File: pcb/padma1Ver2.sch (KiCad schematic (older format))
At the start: 12 parts

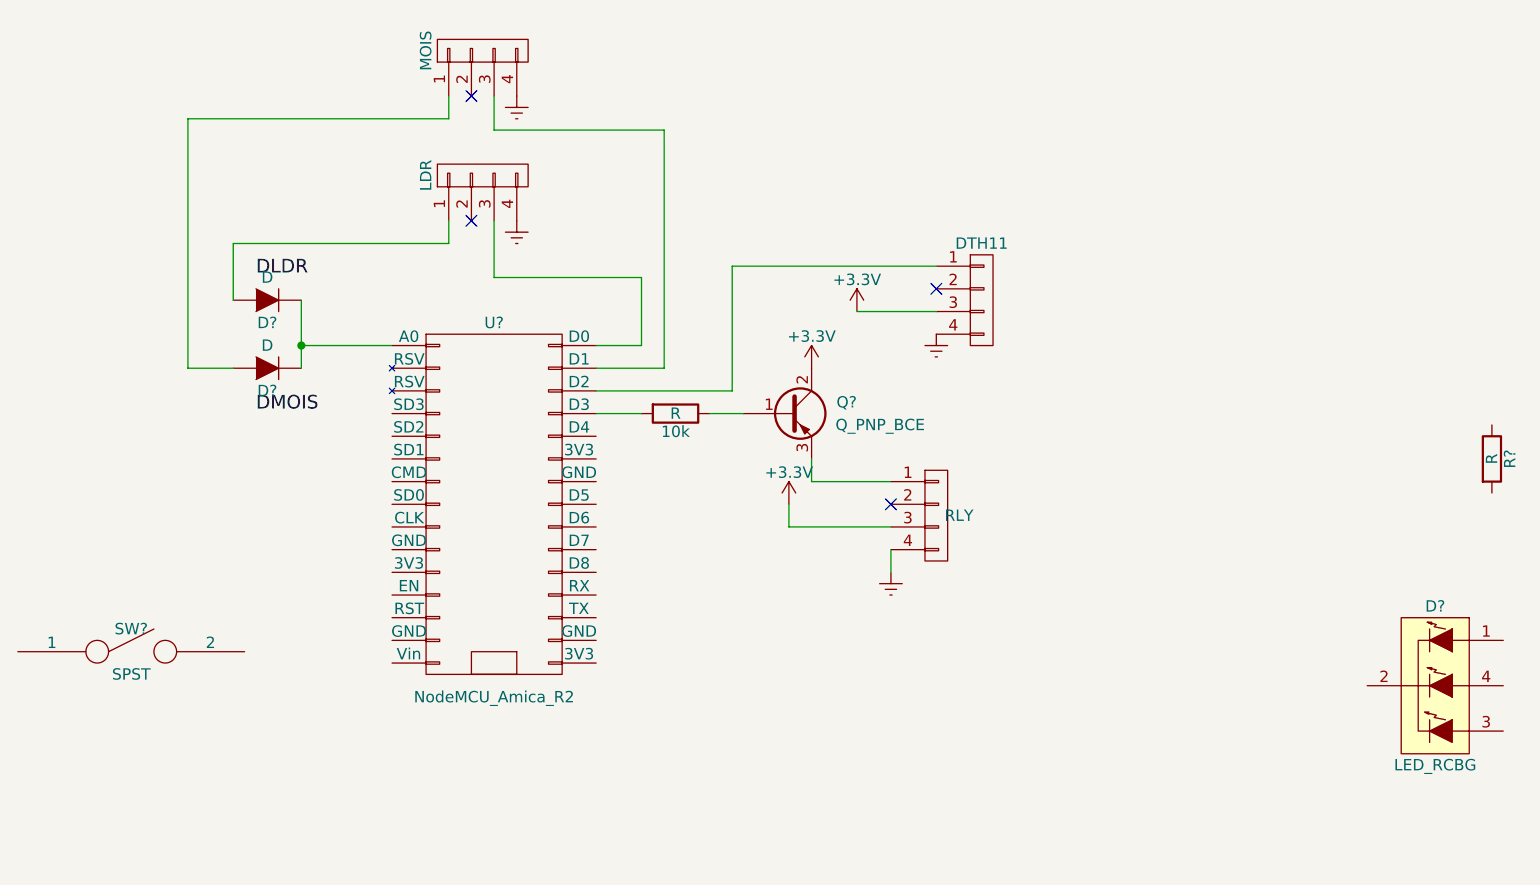
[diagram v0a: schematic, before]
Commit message: schematic completed
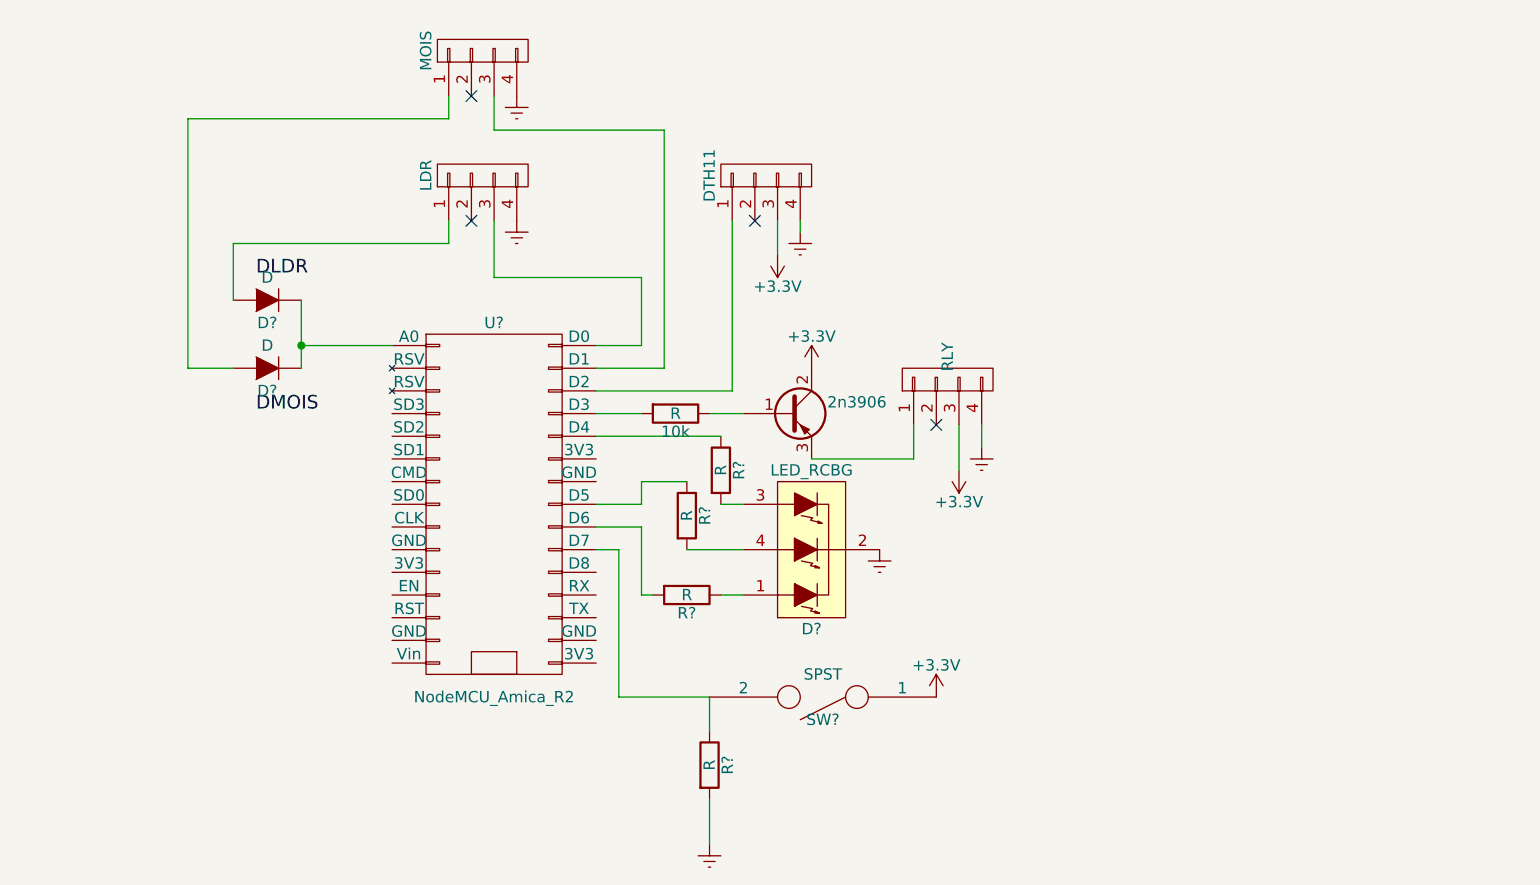
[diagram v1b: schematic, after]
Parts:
- added R? (x3): R, symbol R
- gave numbers to parts that had none: 1
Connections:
- net +3V3: now also SW?.1
- net Earth: now also D?.2 (COMMON_CATHODE), R?.2
- net at U?.21 (D7): now also R?.1, SW?.2
- net at U?.22 (D6): now also R?.2
- net at U?.23 (D5): now also R?.1
- net at U?.26 (D4): now also R?.1
- net at D?.1 (RED_ANODE): now also R?.1
- net at D?.3 (BLUE_ANODE): now also R?.2
- net at D?.4 (GREEN_ANODE): now also R?.2
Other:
- moved on the sheet: D?, DTH11, R?, SW?
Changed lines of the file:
@@
 L R R?
 U 1 1 582C3672
-P 9050 3300
-F 0 "R?" V 9130 3300 50  0000 C CNN
-F 1 "R" V 9050 3300 50  0000 C CNN
-F 2 "" V 8980 3300 50  0000 C CNN
-F 3 "" H 9050 3300 50  0000 C CNN
-	1    9050 3300
+P 5600 4650
+F 0 "R?" V 5680 4650 50  0000 C CNN
+F 1 "R" V 5600 4650 50  0000 C CNN
+F 2 "" V 5530 4650 50  0000 C CNN
+F 3 "" H 5600 4650 50  0000 C CNN
+	1    5600 4650
 	1    0    0    -1
 $EndComp
@@
 $EndComp
 $Comp
-L Q_PNP_BCE Q?
+L Q_PNP_BCE 2n3906
 U 1 1 582C37C4
 P 5950 3100
-F 0 "Q?" H 6250 3150 50  0000 R CNN
-F 1 "Q_PNP_BCE" H 6550 3050 50  0000 R CNN
+F 0 "2n3906" H 6250 3150 50  0000 C CNN
+F 1 "Q_PNP_BCE" H 6550 3050 50  0001 R CNN
 F 2 "" H 6150 3200 50  0000 C CNN
 F 3 "" H 5950 3100 50  0000 C CNN
@@
 L SPST SW?
 U 1 1 582C382D
-P 3050 4150
-F 0 "SW?" H 3050 4250 50  0000 C CNN
-F 1 "SPST" H 3050 4050 50  0000 C CNN
-F 2 "" H 3050 4150 50  0000 C CNN
-F 3 "" H 3050 4150 50  0000 C CNN
-	1    3050 4150
-	1    0    0    -1
-$EndComp
-$Comp
-L LED_RCBG D?
-U 1 1 582C388A
-P 8800 4300
-F 0 "D?" H 8800 4650 50  0000 C CNN
-F 1 "LED_RCBG" H 8800 3950 50  0000 C CNN
-F 2 "" H 8800 4250 50  0000 C CNN
-F 3 "" H 8800 4250 50  0000 C CNN
-	1    8800 4300
-	1    0    0    -1
+P 6100 4350
+F 0 "SW?" H 6100 4450 50  0000 C CNN
+F 1 "SPST" H 6100 4250 50  0000 C CNN
+F 2 "" H 6100 4350 50  0000 C CNN
+F 3 "" H 6100 4350 50  0000 C CNN
+	1    6100 4350
+	-1   0    0    1
 $EndComp
 $Comp
@@
 	-1   0    0    1
 $EndComp
-Wire Wire Line
-	3800 2600 3800 2900
-Wire Wire Line
-	4200 2800 3800 2800
-Connection ~ 3800 2800
 $Comp
 L CONN_01X04 LDR
@@
 L CONN_01X04 DTH11
 U 1 1 582C4013
-P 6800 2600
-F 0 "DTH11" H 6800 2850 50  0000 C CNN
-F 1 "CONN_01X04" V 6900 2600 50  0001 C CNN
-F 2 "" H 6800 2600 50  0000 C CNN
-F 3 "" H 6800 2600 50  0000 C CNN
-	1    6800 2600
-	1    0    0    -1
+P 5850 2050
+F 0 "DTH11" H 5850 2300 50  0000 C CNN
+F 1 "CONN_01X04" V 5950 2050 50  0001 C CNN
+F 2 "" H 5850 2050 50  0000 C CNN
+F 3 "" H 5850 2050 50  0000 C CNN
+	1    5850 2050
+	0    -1   -1   0
 $EndComp
 $Comp
 L CONN_01X04 Grovr
 U 1 1 582C406C
-P 6600 3550
-F 0 "Grovr" H 6600 3800 50  0001 C CNN
-F 1 "RLY" H 6700 3550 50  0000 C CNN
-F 2 "" H 6600 3550 50  0000 C CNN
-F 3 "" H 6600 3550 50  0000 C CNN
-	1    6600 3550
-	1    0    0    -1
+P 6650 2950
+F 0 "Grovr" H 6650 3200 50  0001 C CNN
+F 1 "RLY" H 6750 2950 50  0000 C CNN
+F 2 "" H 6650 2950 50  0000 C CNN
+F 3 "" H 6650 2950 50  0000 C CNN
+	1    6650 2950
+	0    -1   -1   0
 $EndComp
 Text Label 3600 2500 0    60   ~ 0
@@
 Text Label 3600 3100 0    60   ~ 0
 DMOIS
-Wire Wire Line
-	3500 2600 3500 2350
-Wire Wire Line
-	3300 2900 3500 2900
-Wire Wire Line
-	3300 1800 3300 2900
-Wire Wire Line
-	3300 1800 4450 1800
-Wire Wire Line
-	4450 1800 4450 1700
-Wire Wire Line
-	3500 2350 4450 2350
-Wire Wire Line
-	4450 2350 4450 2250
 NoConn ~ 4550 2250
 NoConn ~ 4550 1700
-Wire Wire Line
-	5100 2800 5300 2800
-Wire Wire Line
-	5300 2800 5300 2500
-Wire Wire Line
-	5300 2500 4650 2500
-Wire Wire Line
-	4650 2500 4650 2250
-Wire Wire Line
-	5100 2900 5400 2900
 $Comp
 L Earth #PWR?
@@
 	1    0    0    -1
 $EndComp
-$Comp
-L Earth #PWR?
-U 1 1 582C4E32
-P 6600 2750
-F 0 "#PWR?" H 6600 2500 50  0001 C CNN
-F 1 "Earth" H 6600 2600 50  0001 C CNN
-F 2 "" H 6600 2750 50  0000 C CNN
-F 3 "" H 6600 2750 50  0000 C CNN
-	1    6600 2750
-	1    0    0    -1
-$EndComp
-NoConn ~ 6600 2550
-$Comp
-L +3.3V #PWR?
-U 1 1 582C4FDC
-P 6250 2650
-F 0 "#PWR?" H 6250 2500 50  0001 C CNN
-F 1 "+3.3V" H 6250 2790 50  0000 C CNN
-F 2 "" H 6250 2650 50  0000 C CNN
-F 3 "" H 6250 2650 50  0000 C CNN
-	1    6250 2650
-	1    0    0    -1
-$EndComp
-Wire Wire Line
-	6600 2650 6250 2650
-Wire Wire Line
-	5100 3000 5700 3000
-Wire Wire Line
-	5700 3000 5700 2450
-Wire Wire Line
-	5700 2450 6600 2450
-Wire Wire Line
-	5100 3100 5300 3100
-Wire Wire Line
-	5600 3100 5750 3100
 $Comp
 L +3.3V #PWR?
@@
 	1    0    0    -1
 $EndComp
-Wire Wire Line
-	6050 3300 6050 3400
-Wire Wire Line
-	6050 3400 6400 3400
-Wire Wire Line
-	4650 1700 4650 1850
-Wire Wire Line
-	4650 1850 5400 1850
-Wire Wire Line
-	5400 1850 5400 2900
 $Comp
 L Earth #PWR?
@@
 	1    0    0    -1
 $EndComp
-NoConn ~ 6400 3500
+NoConn ~ 5800 2250
 $Comp
 L +3.3V #PWR?
-U 1 1 582C6CAC
-P 5950 3500
-F 0 "#PWR?" H 5950 3350 50  0001 C CNN
-F 1 "+3.3V" H 5950 3640 50  0000 C CNN
-F 2 "" H 5950 3500 50  0000 C CNN
-F 3 "" H 5950 3500 50  0000 C CNN
-	1    5950 3500
-	1    0    0    -1
-$EndComp
-$Comp
-L Earth #PWR?
-U 1 1 582C6D84
-P 6400 3800
-F 0 "#PWR?" H 6400 3550 50  0001 C CNN
-F 1 "Earth" H 6400 3650 50  0001 C CNN
-F 2 "" H 6400 3800 50  0000 C CNN
-F 3 "" H 6400 3800 50  0000 C CNN
-	1    6400 3800
-	1    0    0    -1
-$EndComp
-Wire Wire Line
-	6400 3700 6400 3800
-Wire Wire Line
-	5950 3600 6400 3600
-Wire Wire Line
-	5950 3500 5950 3600
+U 1 1 582C7499
+P 5900 2400
+F 0 "#PWR?" H 5900 2250 50  0001 C CNN
+F 1 "+3.3V" H 5900 2540 50  0000 C CNN
+F 2 "" H 5900 2400 50  0000 C CNN
+F 3 "" H 5900 2400 50  0000 C CNN
+	1    5900 2400
+	-1   0    0    1
+$EndComp
+$Comp
+L Earth #PWR?
+U 1 1 582C7550
+P 6000 2300
+F 0 "#PWR?" H 6000 2050 50  0001 C CNN
+F 1 "Earth" H 6000 2150 50  0001 C CNN
+F 2 "" H 6000 2300 50  0000 C CNN
+F 3 "" H 6000 2300 50  0000 C CNN
+	1    6000 2300
+	1    0    0    -1
+$EndComp
+NoConn ~ 6600 3150
+$Comp
+L +3.3V #PWR?
+U 1 1 582C78ED
+P 6700 3350
+F 0 "#PWR?" H 6700 3200 50  0001 C CNN
+F 1 "+3.3V" H 6700 3490 50  0000 C CNN
+F 2 "" H 6700 3350 50  0000 C CNN
+F 3 "" H 6700 3350 50  0000 C CNN
+	1    6700 3350
+	-1   0    0    1
+$EndComp
+$Comp
+L Earth #PWR?
+U 1 1 582C79CF
+P 6800 3250
+F 0 "#PWR?" H 6800 3000 50  0001 C CNN
+F 1 "Earth" H 6800 3100 50  0001 C CNN
+F 2 "" H 6800 3250 50  0000 C CNN
+F 3 "" H 6800 3250 50  0000 C CNN
+	1    6800 3250
+	1    0    0    -1
+$EndComp
+$Comp
+L LED_RCBG D?
+U 1 1 582C388A
+P 6050 3700
+F 0 "D?" H 6050 4050 50  0000 C CNN
+F 1 "LED_RCBG" H 6050 3350 50  0000 C CNN
+F 2 "" H 6050 3650 50  0000 C CNN
+F 3 "" H 6050 3650 50  0000 C CNN
+	1    6050 3700
+	-1   0    0    1
+$EndComp
+$Comp
+L R R?
+U 1 1 582C8339
+P 5650 3350
+F 0 "R?" V 5730 3350 50  0000 C CNN
+F 1 "R" V 5650 3350 50  0000 C CNN
+F 2 "" V 5580 3350 50  0000 C CNN
+F 3 "" H 5650 3350 50  0000 C CNN
+	1    5650 3350
+	1    0    0    -1
+$EndComp
+$Comp
+L R R?
+U 1 1 582C866A
+P 5500 3550
+F 0 "R?" V 5580 3550 50  0000 C CNN
+F 1 "R" V 5500 3550 50  0000 C CNN
+F 2 "" V 5430 3550 50  0000 C CNN
+F 3 "" H 5500 3550 50  0000 C CNN
+	1    5500 3550
+	1    0    0    -1
+$EndComp
+$Comp
+L R R?
+U 1 1 582C8997
+P 5500 3900
+F 0 "R?" V 5580 3900 50  0000 C CNN
+F 1 "R" V 5500 3900 50  0000 C CNN
+F 2 "" V 5430 3900 50  0000 C CNN
+F 3 "" H 5500 3900 50  0000 C CNN
+	1    5500 3900
+	0    1    1    0
+$EndComp
+$Comp
+L Earth #PWR?
+U 1 1 582C8C6A
+P 6350 3700
+F 0 "#PWR?" H 6350 3450 50  0001 C CNN
+F 1 "Earth" H 6350 3550 50  0001 C CNN
+F 2 "" H 6350 3700 50  0000 C CNN
+F 3 "" H 6350 3700 50  0000 C CNN
+	1    6350 3700
+	1    0    0    -1
+$EndComp
+Wire Wire Line
+	3800 2600 3800 2900
+Wire Wire Line
+	4200 2800 3800 2800
+Connection ~ 3800 2800
+Wire Wire Line
+	3500 2600 3500 2350
+Wire Wire Line
+	3300 2900 3500 2900
+Wire Wire Line
+	3300 1800 3300 2900
+Wire Wire Line
+	3300 1800 4450 1800
+Wire Wire Line
+	4450 1800 4450 1700
+Wire Wire Line
+	3500 2350 4450 2350
+Wire Wire Line
+	4450 2350 4450 2250
+Wire Wire Line
+	5100 2800 5300 2800
+Wire Wire Line
+	5300 2800 5300 2500
+Wire Wire Line
+	5300 2500 4650 2500
+Wire Wire Line
+	4650 2500 4650 2250
+Wire Wire Line
+	5100 2900 5400 2900
+Wire Wire Line
+	5100 3100 5300 3100
+Wire Wire Line
+	5600 3100 5750 3100
+Wire Wire Line
+	4650 1700 4650 1850
+Wire Wire Line
+	4650 1850 5400 1850
+Wire Wire Line
+	5400 1850 5400 2900
+Wire Wire Line
+	5100 3000 5700 3000
+Wire Wire Line
+	5700 3000 5700 2250
+Wire Wire Line
+	5900 2250 5900 2400
+Wire Wire Line
+	6000 2250 6000 2300
+Wire Wire Line
+	6050 3300 6500 3300
+Wire Wire Line
+	6500 3300 6500 3150
+Wire Wire Line
+	6700 3350 6700 3150
+Wire Wire Line
+	6800 3250 6800 3150
+Wire Wire Line
+	5100 3200 5650 3200
+Wire Wire Line
+	5650 3500 5750 3500
+Wire Wire Line
+	5100 3500 5300 3500
+Wire Wire Line
+	5300 3500 5300 3400
+Wire Wire Line
+	5300 3400 5500 3400
+Wire Wire Line
+	5500 3700 5750 3700
+Wire Wire Line
+	5650 3900 5750 3900
+Wire Wire Line
+	5100 3600 5300 3600
+Wire Wire Line
+	5300 3600 5300 3900
+Wire Wire Line
+	5300 3900 5350 3900
+Wire Wire Line
+	5600 4500 5600 4350
+Wire Wire Line
+	5100 3700 5200 3700
+Wire Wire Line
+	5200 3700 5200 4350
+Wire Wire Line
+	5200 4350 5600 4350
+$Comp
+L Earth #PWR?
+U 1 1 582C92CF
+P 5600 5000
+F 0 "#PWR?" H 5600 4750 50  0001 C CNN
+F 1 "Earth" H 5600 4850 50  0001 C CNN
+F 2 "" H 5600 5000 50  0000 C CNN
+F 3 "" H 5600 5000 50  0000 C CNN
+	1    5600 5000
+	1    0    0    -1
+$EndComp
+Wire Wire Line
+	5600 5000 5600 4800
+$Comp
+L +3.3V #PWR?
+U 1 1 582C937E
+P 6600 4350
+F 0 "#PWR?" H 6600 4200 50  0001 C CNN
+F 1 "+3.3V" H 6600 4490 50  0000 C CNN
+F 2 "" H 6600 4350 50  0000 C CNN
+F 3 "" H 6600 4350 50  0000 C CNN
+	1    6600 4350
+	1    0    0    -1
+$EndComp
 $EndSCHEMATC

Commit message: added layout
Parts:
- gave numbers to parts that had none: 9
- renumbered 10k to 10k1, Grovr to Grovr1, LDR to LDR1, MOIS to MOIS1
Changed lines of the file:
@@
 $EndDescr
 $Comp
-L NodeMCU_Amica_R2 U?
+L NodeMCU_Amica_R2 U1
 U 1 1 582C3605
 P 4650 3500
-F 0 "U?" H 4650 4300 50  0000 C CNN
+F 0 "U1" H 4650 4300 50  0000 C CNN
 F 1 "NodeMCU_Amica_R2" H 4650 2650 50  0000 C CNN
 F 2 "" H 4900 3500 50  0000 C CNN
@@
 $EndComp
 $Comp
-L R R?
+L R R3
 U 1 1 582C3672
 P 5600 4650
-F 0 "R?" V 5680 4650 50  0000 C CNN
+F 0 "R3" V 5680 4650 50  0000 C CNN
 F 1 "R" V 5600 4650 50  0000 C CNN
 F 2 "" V 5530 4650 50  0000 C CNN
@@
 $EndComp
 $Comp
-L R 10k
+L R 10k1
 U 1 1 582C36F9
 P 5450 3100
-F 0 "10k" V 5530 3100 50  0000 C CNN
+F 0 "10k1" V 5530 3100 50  0000 C CNN
 F 1 "R" V 5450 3100 50  0000 C CNN
 F 2 "" V 5380 3100 50  0000 C CNN
@@
 $EndComp
 $Comp
-L D D?
+L D D2
 U 1 1 582C376F
 P 3650 2900
-F 0 "D?" H 3650 3000 50  0000 C CNN
+F 0 "D2" H 3650 3000 50  0000 C CNN
 F 1 "D" H 3650 2800 50  0000 C CNN
 F 2 "" H 3650 2900 50  0000 C CNN
@@
 $EndComp
 $Comp
-L SPST SW?
+L SPST SW1
 U 1 1 582C382D
 P 6100 4350
-F 0 "SW?" H 6100 4450 50  0000 C CNN
+F 0 "SW1" H 6100 4450 50  0000 C CNN
 F 1 "SPST" H 6100 4250 50  0000 C CNN
 F 2 "" H 6100 4350 50  0000 C CNN
@@
 $EndComp
 $Comp
-L D D?
+L D D1
 U 1 1 582C3A72
 P 3650 2600
-F 0 "D?" H 3650 2700 50  0000 C CNN
+F 0 "D1" H 3650 2700 50  0000 C CNN
 F 1 "D" H 3650 2500 50  0000 C CNN
 F 2 "" H 3650 2600 50  0000 C CNN
@@
 $EndComp
 $Comp
-L CONN_01X04 LDR
+L CONN_01X04 LDR1
 U 1 1 582C3F02
 P 4600 2050
-F 0 "LDR" H 4600 2300 50  0000 C CNN
+F 0 "LDR1" H 4600 2300 50  0000 C CNN
 F 1 "CONN_01X04" V 4700 2050 50  0001 C CNN
 F 2 "" H 4600 2050 50  0000 C CNN
@@
 $EndComp
 $Comp
-L CONN_01X04 MOIS
+L CONN_01X04 MOIS1
 U 1 1 582C3F9A
 P 4600 1500
-F 0 "MOIS" H 4600 1750 50  0000 C CNN
+F 0 "MOIS1" H 4600 1750 50  0000 C CNN
 F 1 "CONN_01X04" V 4700 1500 50  0001 C CNN
 F 2 "" H 4600 1500 50  0000 C CNN
@@
 $EndComp
 $Comp
-L CONN_01X04 Grovr
+L CONN_01X04 Grovr1
 U 1 1 582C406C
 P 6650 2950
-F 0 "Grovr" H 6650 3200 50  0001 C CNN
+F 0 "Grovr1" H 6650 3200 50  0001 C CNN
 F 1 "RLY" H 6750 2950 50  0000 C CNN
 F 2 "" H 6650 2950 50  0000 C CNN
@@
 NoConn ~ 4550 1700
 $Comp
-L Earth #PWR?
+L Earth #PWR2
 U 1 1 582C4AC2
 P 4750 2250
-F 0 "#PWR?" H 4750 2000 50  0001 C CNN
+F 0 "#PWR2" H 4750 2000 50  0001 C CNN
 F 1 "Earth" H 4750 2100 50  0001 C CNN
 F 2 "" H 4750 2250 50  0000 C CNN
@@
 $EndComp
 $Comp
-L +3.3V #PWR?
+L +3.3V #PWR6
 U 1 1 582C5C13
 P 6050 2900
-F 0 "#PWR?" H 6050 2750 50  0001 C CNN
+F 0 "#PWR6" H 6050 2750 50  0001 C CNN
 F 1 "+3.3V" H 6050 3040 50  0000 C CNN
 F 2 "" H 6050 2900 50  0000 C CNN
@@
 $EndComp
 $Comp
-L Earth #PWR?
+L Earth #PWR1
 U 1 1 582C693C
 P 4750 1700
-F 0 "#PWR?" H 4750 1450 50  0001 C CNN
+F 0 "#PWR1" H 4750 1450 50  0001 C CNN
 F 1 "Earth" H 4750 1550 50  0001 C CNN
 F 2 "" H 4750 1700 50  0000 C CNN
@@
 NoConn ~ 5800 2250
 $Comp
-L +3.3V #PWR?
+L +3.3V #PWR4
 U 1 1 582C7499
 P 5900 2400
-F 0 "#PWR?" H 5900 2250 50  0001 C CNN
+F 0 "#PWR4" H 5900 2250 50  0001 C CNN
 F 1 "+3.3V" H 5900 2540 50  0000 C CNN
 F 2 "" H 5900 2400 50  0000 C CNN
@@
 $EndComp
 $Comp
-L Earth #PWR?
+L Earth #PWR5
 U 1 1 582C7550
 P 6000 2300
-F 0 "#PWR?" H 6000 2050 50  0001 C CNN
+F 0 "#PWR5" H 6000 2050 50  0001 C CNN
 F 1 "Earth" H 6000 2150 50  0001 C CNN
 F 2 "" H 6000 2300 50  0000 C CNN
@@
 NoConn ~ 6600 3150
 $Comp
-L +3.3V #PWR?
+L +3.3V #PWR9
 U 1 1 582C78ED
 P 6700 3350
-F 0 "#PWR?" H 6700 3200 50  0001 C CNN
+F 0 "#PWR9" H 6700 3200 50  0001 C CNN
 F 1 "+3.3V" H 6700 3490 50  0000 C CNN
 F 2 "" H 6700 3350 50  0000 C CNN
@@
 $EndComp
 $Comp
-L Earth #PWR?
+L Earth #PWR10
 U 1 1 582C79CF
 P 6800 3250
-F 0 "#PWR?" H 6800 3000 50  0001 C CNN
+F 0 "#PWR10" H 6800 3000 50  0001 C CNN
 F 1 "Earth" H 6800 3100 50  0001 C CNN
 F 2 "" H 6800 3250 50  0000 C CNN
@@
 $EndComp
 $Comp
-L LED_RCBG D?
+L LED_RCBG D3
 U 1 1 582C388A
 P 6050 3700
-F 0 "D?" H 6050 4050 50  0000 C CNN
+F 0 "D3" H 6050 4050 50  0000 C CNN
 F 1 "LED_RCBG" H 6050 3350 50  0000 C CNN
 F 2 "" H 6050 3650 50  0000 C CNN
@@
 $EndComp
 $Comp
-L R R?
+L R R4
 U 1 1 582C8339
 P 5650 3350
-F 0 "R?" V 5730 3350 50  0000 C CNN
+F 0 "R4" V 5730 3350 50  0000 C CNN
 F 1 "R" V 5650 3350 50  0000 C CNN
 F 2 "" V 5580 3350 50  0000 C CNN
@@
 $EndComp
 $Comp
-L R R?
+L R R1
 U 1 1 582C866A
 P 5500 3550
-F 0 "R?" V 5580 3550 50  0000 C CNN
+F 0 "R1" V 5580 3550 50  0000 C CNN
 F 1 "R" V 5500 3550 50  0000 C CNN
 F 2 "" V 5430 3550 50  0000 C CNN
@@
 $EndComp
 $Comp
-L R R?
+L R R2
 U 1 1 582C8997
 P 5500 3900
-F 0 "R?" V 5580 3900 50  0000 C CNN
+F 0 "R2" V 5580 3900 50  0000 C CNN
 F 1 "R" V 5500 3900 50  0000 C CNN
 F 2 "" V 5430 3900 50  0000 C CNN
@@
 $EndComp
 $Comp
-L Earth #PWR?
+L Earth #PWR7
 U 1 1 582C8C6A
 P 6350 3700
-F 0 "#PWR?" H 6350 3450 50  0001 C CNN
+F 0 "#PWR7" H 6350 3450 50  0001 C CNN
 F 1 "Earth" H 6350 3550 50  0001 C CNN
 F 2 "" H 6350 3700 50  0000 C CNN
@@
 	5200 4350 5600 4350
 $Comp
-L Earth #PWR?
+L Earth #PWR3
 U 1 1 582C92CF
 P 5600 5000
-F 0 "#PWR?" H 5600 4750 50  0001 C CNN
+F 0 "#PWR3" H 5600 4750 50  0001 C CNN
 F 1 "Earth" H 5600 4850 50  0001 C CNN
 F 2 "" H 5600 5000 50  0000 C CNN
@@
 	5600 5000 5600 4800
 $Comp
-L +3.3V #PWR?
+L +3.3V #PWR8
 U 1 1 582C937E
 P 6600 4350
-F 0 "#PWR?" H 6600 4200 50  0001 C CNN
+F 0 "#PWR8" H 6600 4200 50  0001 C CNN
 F 1 "+3.3V" H 6600 4490 50  0000 C CNN
 F 2 "" H 6600 4350 50  0000 C CNN
